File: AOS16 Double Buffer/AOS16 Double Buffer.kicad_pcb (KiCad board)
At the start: 4 copper layers, 47 x 72 mm, 50 parts, among them IC1 IS61WV3216BLL-12TLI, IC2 SN74LVC16245ADGVR, IC3 SN74LVC16245ADGVR, IC4 SN74LVC16245ADGVR, IC5 SN74LVC16245ADGVR, J1 Conn_01x02_Pin, J2 Conn_02x08_Top_Bottom, J3 Conn_02x08_Top_Bottom, J4 Conn_02x08_Top_Bottom, J5 Conn_02x08_Top_Bottom, J6 Conn_01x07_Pin, U1 74AHC1G08, U2 74AHC1G08, U3 74AHC1G32, U4 74AHC1G32, U5 74AHC1G04, U6 74AHC1G04, U7 74LS157

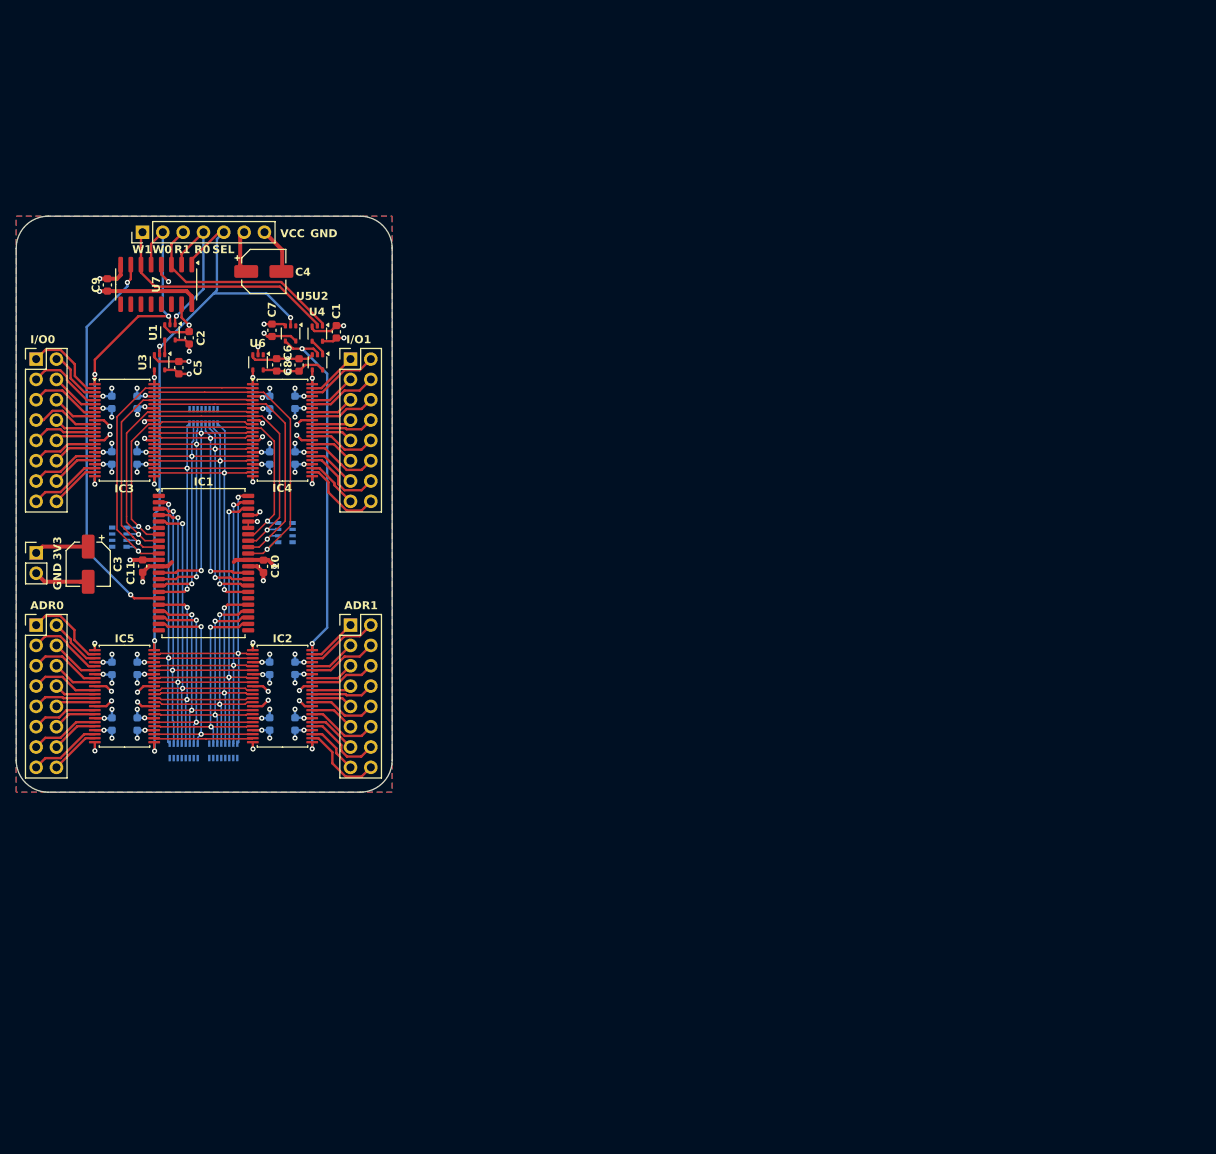
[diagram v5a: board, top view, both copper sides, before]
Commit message: Fixed double buffer logic families
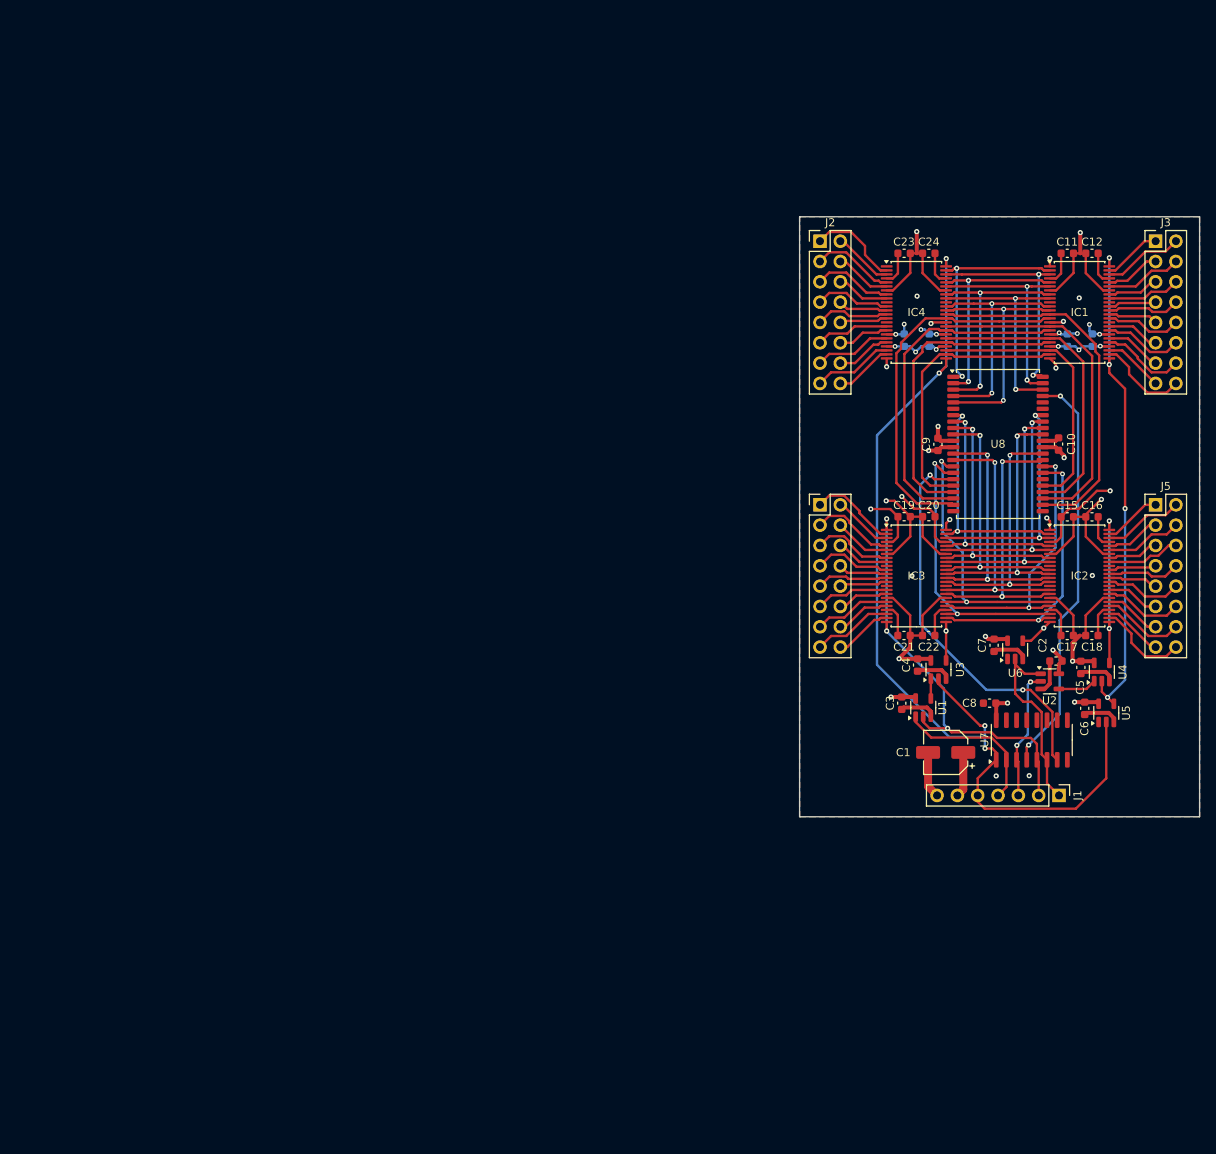
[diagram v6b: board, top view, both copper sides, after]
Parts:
- removed C27: 0.01uF, Capacitor_SMD:C_0603_1608Metric
- removed IC5: SN74LVC16245ADGVR, Package_SO:TSSOP-48_6.1x12.5mm_P0.5mm
- removed J6: Conn_01x07_Pin, Connector_PinHeader_2.54mm:PinHeader_1x07_P2.54mm_Vertical
- removed RN1, RN2, RN5: R_Pack08, Resistor_SMD:R_Array_Convex_8x0602
- removed RN3, RN4: R_Pack04, Resistor_SMD:R_Array_Convex_4x0603
- added U8: 71016S12PHG8, Package_SO:TSOP-II-44_10.16x18.41mm_P0.8mm, F.Cu at (146.7, 78.5)
- C1: value 0.1uF -> 100 uF; footprint Capacitor_SMD:C_0603_1608Metric -> Capacitor_SMD:CP_Elec_5x5.3
- C11: value 0.1uF -> 0.01uF
- C12, C15, C16, C17, C18, C19, C20, C21, C22, C23, C24: moved to F.Cu
- C3, C4: value 100 uF -> 0.1uF; footprint Capacitor_SMD:CP_Elec_5x5.3 -> Capacitor_SMD:C_0603_1608Metric
- IC1: value IS61WV3216BLL-12TLI -> SN74AHCT16245ADGGR; footprint Package_SO:TSOP-II-44_10.16x18.41mm_P0.8mm -> Package_SO:TSSOP-48_6.1x12.5mm_P0.5mm
- IC2, IC3, IC4: value SN74LVC16245ADGVR -> SN74AHCT16245ADGGR
- J1: value Conn_01x02_Pin -> Conn_01x07_Pin; footprint Connector_PinHeader_2.54mm:PinHeader_1x02_P2.54mm_Vertical -> Connector_PinHeader_2.54mm:PinHeader_1x07_P2.54mm_Vertical
- U1, U2: value 74AHC1G08 -> 74AHCT1G08; footprint Package_TO_SOT_SMD:SOT-353_SC-70-5 -> Package_TO_SOT_SMD:SOT-23-5
- U3, U4: value 74AHC1G32 -> 74AHCT1G32; footprint Package_TO_SOT_SMD:SOT-353_SC-70-5 -> Package_TO_SOT_SMD:SOT-23-5
- U5, U6: value 74AHC1G04 -> 74AHCT1G04; footprint Package_TO_SOT_SMD:SOT-353_SC-70-5 -> Package_TO_SOT_SMD:SOT-23-5
- U7: value 74LS157 -> 74LVC157
- moved J1 131.4 mm to (154.3, 122.4), turned to -90 degrees
- moved C18 124.5 mm to (158.5, 102.4), turned to 0 degrees
- moved U7 123.4 mm to (150.9, 115.5), turned to 90 degrees
- moved C16 123.4 mm to (158.5, 87.6), turned to 0 degrees
- moved C11 122.0 mm to (155.4, 54.6), turned to 180 degrees
- moved C17 119.9 mm to (155.4, 102.4), turned to 180 degrees
- moved C5 118.8 mm to (157.1, 106.4), turned to -90 degrees
- moved C2 115.6 mm to (154.0, 105.6), turned to 180 degrees
- moved C12 115.1 mm to (158.5, 54.6), turned to 0 degrees
- moved C24 114.5 mm to (138.1, 54.6), turned to 0 degrees
- moved IC1 113.9 mm to (156.9, 62.0)
- moved C14 113.5 mm to (158.5, 65.5)
- moved U5 112.4 mm to (160.3, 112.1), turned to 90 degrees
- moved J3 111.5 mm to (166.4, 53.1)
- moved C26 110.0 mm to (135.0, 65.5)
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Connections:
- C1 pad 1: VCC -> +5V
- C10 pad 1: +3.3V -> +5V
- C11 pad 1: +3.3V -> +5V
- C12 pad 1: +3.3V -> +5V
- C13 pad 1: +3.3V -> +5V
- C14 pad 1: +3.3V -> +5V
- C15 pad 1: +3.3V -> +5V
- C16 pad 1: +3.3V -> +5V
- C17 pad 1: +3.3V -> +5V
- C18 pad 1: +3.3V -> +5V
- C19 pad 1: +3.3V -> +5V
- C2 pad 1: VCC -> +5V
- C20 pad 1: +3.3V -> +5V
- C21 pad 1: +3.3V -> +5V
- C22 pad 1: +3.3V -> +5V
- C23 pad 1: +3.3V -> +5V
- C24 pad 1: +3.3V -> +5V
- C25 pad 1: +3.3V -> +5V
- C26 pad 1: +3.3V -> +5V
- C3 pad 1: +3.3V -> +5V
- C4 pad 1: VCC -> +5V
- C5 pad 1: VCC -> +5V
- C6 pad 1: VCC -> +5V
- C7 pad 1: VCC -> +5V
- C8 pad 1: VCC -> +5V
- C9 pad 1: VCC -> +5V
- IC1 pad 1: unconnected-(IC1-NC_1-Pad1) -> +5V
- IC1 pad 10: /ram/OUT0 -> GND
- IC1 pad 11: +3.3V -> /ram/INA6
- IC1 pad 12: GND -> /ram/INA7
- IC1 pad 13: /ram/OUT8 -> /ram/INA8
- IC1 pad 14: /ram/OUT10 -> /ram/INA9
- IC1 pad 15: /ram/OUT12 -> GND
- IC1 pad 16: /ram/OUT14 -> /ram/INA10
- IC1 pad 17: /W -> /ram/INA11
- IC1 pad 18: /pull_resistor/IN8 -> +5V
- IC1 pad 19: /pull_resistor/IN10 -> /ram/INA12
- IC1 pad 2: /pull_resistor/IN1 -> /ram/INA0
- IC1 pad 20: /pull_resistor/IN12 -> /ram/INA13
- IC1 pad 21: /pull_resistor/IN14 -> GND
- IC1 pad 22: unconnected-(IC1-NC_2-Pad22) -> /ram/INA14
- IC1 pad 23: unconnected-(IC1-NC_3-Pad23) -> /ram/INA15
- IC1 pad 24: /pull_resistor/IN13 -> +5V
- IC1 pad 25: /pull_resistor/IN11 -> /~{SEL}
- IC1 pad 26: /pull_resistor/IN9 -> /word_conn1/IN15
- IC1 pad 27: /pull_resistor/IN7 -> /word_conn1/IN14
- IC1 pad 28: unconnected-(IC1-NC_4-Pad28) -> GND
- IC1 pad 29: /ram/OUT15 -> /word_conn1/IN13
- IC1 pad 3: /pull_resistor/IN3 -> /ram/INA1
- IC1 pad 30: /ram/OUT13 -> /word_conn1/IN12
- IC1 pad 31: /ram/OUT11 -> +5V
- IC1 pad 32: /ram/OUT9 -> /word_conn1/IN11
- IC1 pad 33: +3.3V -> /word_conn1/IN10
- IC1 pad 35: /ram/OUT1 -> /word_conn1/IN9
- IC1 pad 36: /ram/OUT3 -> /word_conn1/IN8
- IC1 pad 37: /ram/OUT5 -> /word_conn1/IN7
- IC1 pad 38: /ram/OUT7 -> /word_conn1/IN6
- IC1 pad 4: /pull_resistor/IN5 -> GND
- IC1 pad 40: GND -> /word_conn1/IN5
- IC1 pad 41: /R -> /word_conn1/IN4
- IC1 pad 42: /pull_resistor/IN4 -> +5V
- IC1 pad 43: /pull_resistor/IN2 -> /word_conn1/IN3
- IC1 pad 44: /pull_resistor/IN0 -> /word_conn1/IN2
- IC1 pad 5: /pull_resistor/IN6 -> /ram/INA2
- IC1 pad 6: GND -> /ram/INA3
- IC1 pad 7: /ram/OUT6 -> +5V
- IC1 pad 8: /ram/OUT4 -> /ram/INA4
- IC1 pad 9: /ram/OUT2 -> /ram/INA5
- IC2 pad 1: +3.3V -> /W1
- IC2 pad 11: /pull_resistor/IN6 -> /ram/IO6
- IC2 pad 12: /pull_resistor/IN7 -> /ram/IO7
- IC2 pad 13: /pull_resistor/IN8 -> /ram/IO8
- IC2 pad 14: /pull_resistor/IN9 -> /ram/IO9
- IC2 pad 16: /pull_resistor/IN10 -> /ram/IO10
- IC2 pad 17: /pull_resistor/IN11 -> /ram/IO11
- IC2 pad 18: +3.3V -> +5V
- IC2 pad 19: /pull_resistor/IN12 -> /ram/IO12
- IC2 pad 2: /pull_resistor/IN0 -> /ram/IO0
- IC2 pad 20: /pull_resistor/IN13 -> /ram/IO13
- IC2 pad 22: /pull_resistor/IN14 -> /ram/IO14
- IC2 pad 23: /pull_resistor/IN15 -> /ram/IO15
- IC2 pad 24: +3.3V -> /W1
- IC2 pad 25: /~{SEL} -> /E1
- IC2 pad 26: /word_conn1/IN15 -> /word_conn3/IN15
- IC2 pad 27: /word_conn1/IN14 -> /word_conn3/IN14
- IC2 pad 29: /word_conn1/IN13 -> /word_conn3/IN13
- IC2 pad 3: /pull_resistor/IN1 -> /ram/IO1
- IC2 pad 30: /word_conn1/IN12 -> /word_conn3/IN12
- IC2 pad 31: +3.3V -> +5V
- IC2 pad 32: /word_conn1/IN11 -> /word_conn3/IN11
- IC2 pad 33: /word_conn1/IN10 -> /word_conn3/IN10
- IC2 pad 35: /word_conn1/IN9 -> /word_conn3/IN9
- IC2 pad 36: /word_conn1/IN8 -> /word_conn3/IN8
- IC2 pad 37: /word_conn1/IN7 -> /word_conn3/IN7
- IC2 pad 38: /word_conn1/IN6 -> /word_conn3/IN6
- IC2 pad 40: /word_conn1/IN5 -> /word_conn3/IN5
- IC2 pad 41: /word_conn1/IN4 -> /word_conn3/IN4
- IC2 pad 42: +3.3V -> +5V
- IC2 pad 43: /word_conn1/IN3 -> /word_conn3/IN3
- IC2 pad 44: /word_conn1/IN2 -> /word_conn3/IN2
- IC2 pad 46: /word_conn1/IN1 -> /word_conn3/IN1
- IC2 pad 47: /word_conn1/IN0 -> /word_conn3/IN0
- IC2 pad 48: /~{SEL} -> /E1
- IC2 pad 5: /pull_resistor/IN2 -> /ram/IO2
- IC2 pad 6: /pull_resistor/IN3 -> /ram/IO3
- IC2 pad 7: +3.3V -> +5V
- IC2 pad 8: /pull_resistor/IN4 -> /ram/IO4
- IC2 pad 9: /pull_resistor/IN5 -> /ram/IO5
- IC3 pad 1: /W0 -> /~{W0}
- IC3 pad 18: +3.3V -> +5V
- IC3 pad 24: /W0 -> /~{W0}
- IC3 pad 26: /ram/OUT15 -> /ram/IO15
- IC3 pad 27: /ram/OUT14 -> /ram/IO14
- IC3 pad 29: /ram/OUT13 -> /ram/IO13
- IC3 pad 30: /ram/OUT12 -> /ram/IO12
- IC3 pad 31: +3.3V -> +5V
- IC3 pad 32: /ram/OUT11 -> /ram/IO11
- IC3 pad 33: /ram/OUT10 -> /ram/IO10
- IC3 pad 35: /ram/OUT9 -> /ram/IO9
- IC3 pad 36: /ram/OUT8 -> /ram/IO8
- IC3 pad 37: /ram/OUT7 -> /ram/IO7
- IC3 pad 38: /ram/OUT6 -> /ram/IO6
- IC3 pad 40: /ram/OUT5 -> /ram/IO5
- IC3 pad 41: /ram/OUT4 -> /ram/IO4
- IC3 pad 42: +3.3V -> +5V
- IC3 pad 43: /ram/OUT3 -> /ram/IO3
- IC3 pad 44: /ram/OUT2 -> /ram/IO2
- IC3 pad 46: /ram/OUT1 -> /ram/IO1
- IC3 pad 47: /ram/OUT0 -> /ram/IO0
- IC3 pad 7: +3.3V -> +5V
- IC4 pad 1: /~{W1} -> GND
- IC4 pad 11: /ram/OUT6 -> /word_conn/IN6
- IC4 pad 12: /ram/OUT7 -> /word_conn/IN7
- IC4 pad 13: /ram/OUT8 -> /word_conn/IN8
- IC4 pad 14: /ram/OUT9 -> /word_conn/IN9
- IC4 pad 16: /ram/OUT10 -> /word_conn/IN10
- IC4 pad 17: /ram/OUT11 -> /word_conn/IN11
- IC4 pad 18: +3.3V -> +5V
- IC4 pad 19: /ram/OUT12 -> /word_conn/IN12
- IC4 pad 2: /ram/OUT0 -> /word_conn/IN0
- IC4 pad 20: /ram/OUT13 -> /word_conn/IN13
- IC4 pad 22: /ram/OUT14 -> /word_conn/IN14
- IC4 pad 23: /ram/OUT15 -> /word_conn/IN15
- IC4 pad 24: /~{W1} -> GND
- IC4 pad 25: /E1 -> /SEL
- IC4 pad 26: /word_conn3/IN15 -> /ram/INA15
- IC4 pad 27: /word_conn3/IN14 -> /ram/INA14
- IC4 pad 29: /word_conn3/IN13 -> /ram/INA13
- IC4 pad 3: /ram/OUT1 -> /word_conn/IN1
- IC4 pad 30: /word_conn3/IN12 -> /ram/INA12
- IC4 pad 31: +3.3V -> +5V
- IC4 pad 32: /word_conn3/IN11 -> /ram/INA11
- IC4 pad 33: /word_conn3/IN10 -> /ram/INA10
- IC4 pad 35: /word_conn3/IN9 -> /ram/INA9
- IC4 pad 36: /word_conn3/IN8 -> /ram/INA8
- IC4 pad 37: /word_conn3/IN7 -> /ram/INA7
- IC4 pad 38: /word_conn3/IN6 -> /ram/INA6
- IC4 pad 40: /word_conn3/IN5 -> /ram/INA5
- IC4 pad 41: /word_conn3/IN4 -> /ram/INA4
- IC4 pad 42: +3.3V -> +5V
- IC4 pad 43: /word_conn3/IN3 -> /ram/INA3
- IC4 pad 44: /word_conn3/IN2 -> /ram/INA2
- IC4 pad 46: /word_conn3/IN1 -> /ram/INA1
- IC4 pad 47: /word_conn3/IN0 -> /ram/INA0
- IC4 pad 48: /E1 -> /SEL
- IC4 pad 5: /ram/OUT2 -> /word_conn/IN2
- IC4 pad 6: /ram/OUT3 -> /word_conn/IN3
- IC4 pad 7: +3.3V -> +5V
- IC4 pad 8: /ram/OUT4 -> /word_conn/IN4
- IC4 pad 9: /ram/OUT5 -> /word_conn/IN5
- J1 pad 1: +3.3V -> /~{W1}
- J1 pad 2: GND -> /~{W0}
- U1 pad 1: /R0 -> /~{R0}
- U1 pad 2: /W0 -> /~{W0}
- U1 pad 5: VCC -> +5V
- U2 pad 1: /R1 -> /~{W1}
- U2 pad 2: /W1 -> /~{R1}
- U2 pad 5: VCC -> +5V
- U3 pad 5: VCC -> +5V
- U4 pad 5: VCC -> +5V
- U5 pad 5: VCC -> +5V
- U6 pad 2: /W1 -> /~{W1}
- U6 pad 4: /~{W1} -> /W1
- U6 pad 5: VCC -> +5V
- U7 pad 10: unconnected-(U7-I1c-Pad10) -> GND
- U7 pad 11: unconnected-(U7-I0c-Pad11) -> GND
- U7 pad 13: unconnected-(U7-I1d-Pad13) -> GND
- U7 pad 14: unconnected-(U7-I0d-Pad14) -> GND
- U7 pad 16: VCC -> +5V
- U7 pad 2: /R0 -> /~{R0}
- U7 pad 3: /R1 -> /~{R1}
- U7 pad 4: /R -> /~{R}
- U7 pad 5: /W0 -> /~{W0}
- U7 pad 6: /W1 -> /~{W1}
- U7 pad 7: /W -> /~{W}
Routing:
- net +5V: track 0.00 -> 156.7 mm, vias 0 -> 23
- net +3.3V: track 66.7 -> 0.00 mm, vias 36 -> 0
- net /~{W0}: track 0.00 -> 54.4 mm, vias 0 -> 3
- net /~{R}: track 0.00 -> 51.3 mm, vias 0 -> 2
- net /~{W}: track 0.00 -> 49.5 mm, vias 0 -> 2
- net /W: track 49.5 -> 0.00 mm, vias 2 -> 0
- net /ram/INA9: track 0.00 -> 46.2 mm
- net /ram/INA8: track 0.00 -> 45.9 mm
- net /W0: track 45.8 -> 0.00 mm, vias 3 -> 0
- net /pull_resistor/IN0: track 44.6 -> 0.00 mm, vias 2 -> 0
- net /pull_resistor/IN2: track 44.2 -> 0.00 mm, vias 2 -> 0
- net /pull_resistor/IN4: track 44.0 -> 0.00 mm, vias 2 -> 0
- net /pull_resistor/IN1: track 43.7 -> 0.00 mm, vias 2 -> 0
- net /pull_resistor/IN3: track 43.4 -> 0.00 mm, vias 2 -> 0
- net /pull_resistor/IN5: track 43.3 -> 0.00 mm, vias 2 -> 0
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- added copper zone on In1.Cu, net +5V
- added copper zone on In2.Cu, net GND
- removed copper zone on In2.Cu, net +3.3V
- removed copper zone on In1.Cu, net GND
- removed copper zone on In2.Cu, net VCC
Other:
- board size 47 x 72 mm -> 50 x 75 mm
- board text removed: "3V3"
- board text removed: "ADR0"
- board text removed: "ADR1"
- board text removed: "GND"
- board text removed: "I/O0"
- board text removed: "I/O1"
- board text removed: "R0"
- board text removed: "R1"
- board text removed: "SEL"
- board text removed: "VCC"
- board text removed: "W0"
- board text removed: "W1"

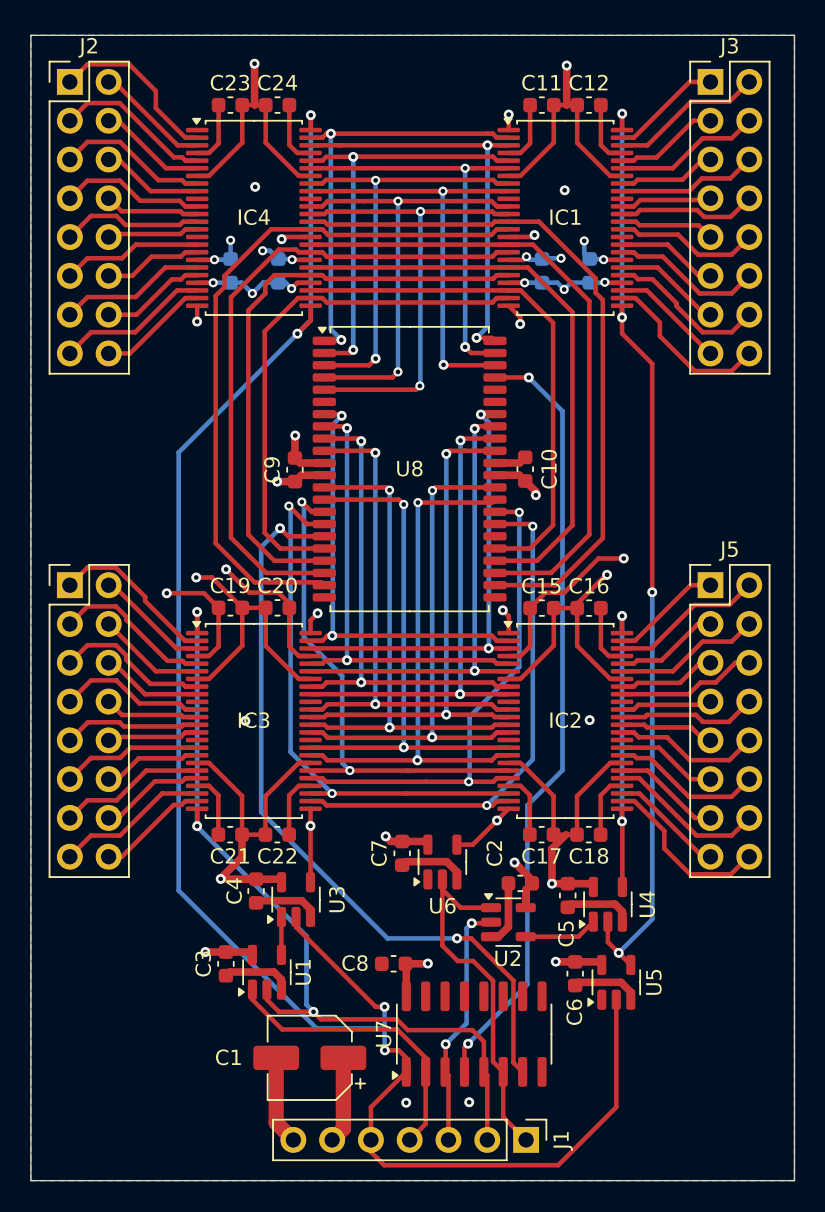
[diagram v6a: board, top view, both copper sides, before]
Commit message: Fixed tri-state buffer and completed double buffer PCB
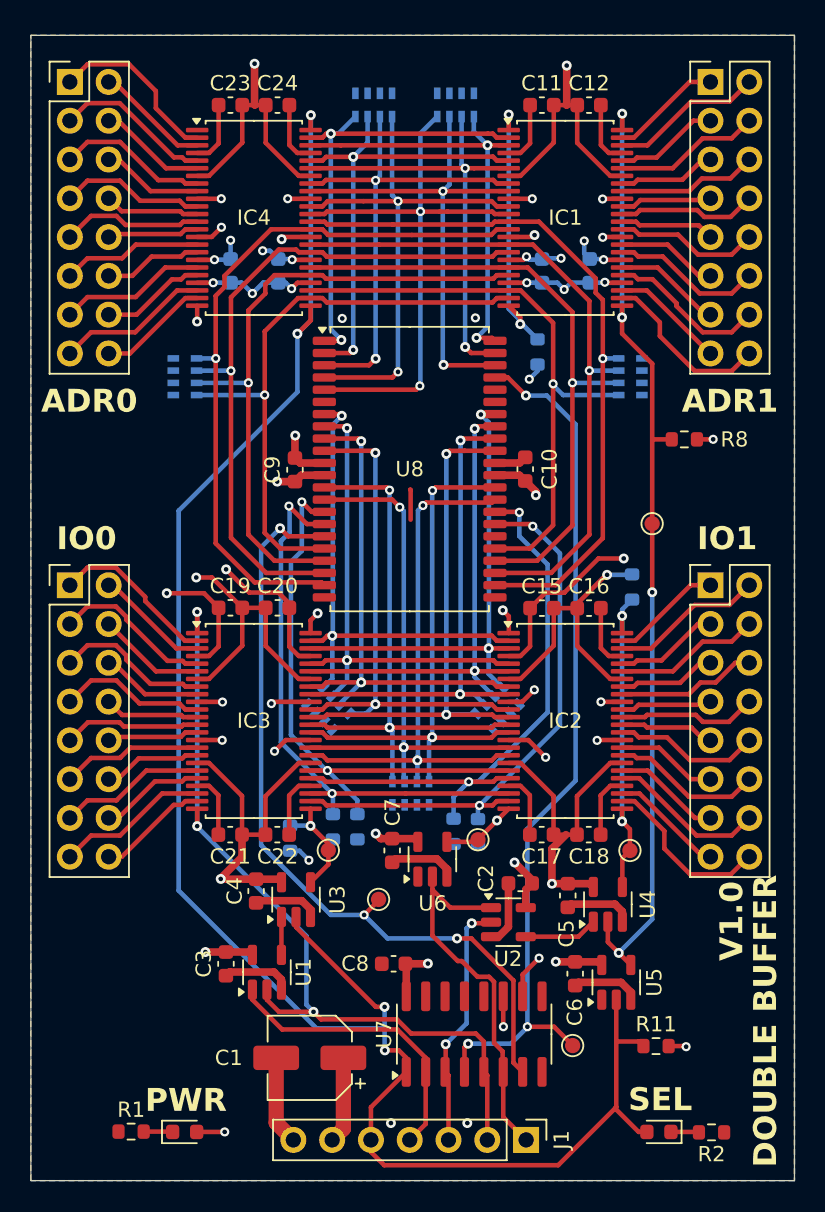
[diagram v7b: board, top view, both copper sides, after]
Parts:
- added D1: LED, LED_SMD:LED_0603_1608Metric, F.Cu at (132.0, 121.9)
- added D2: LED, LED_SMD:LED_0603_1608Metric, F.Cu at (163.0, 121.9)
- added R1: 100, Resistor_SMD:R_0603_1608Metric, F.Cu at (128.5, 121.9)
- added R10: 1k, Resistor_SMD:R_0603_1608Metric, B.Cu at (138.9, 102.6)
- added R11: 1k, Resistor_SMD:R_0603_1608Metric, F.Cu at (162.9, 116.3)
- added R2: 100, Resistor_SMD:R_0603_1608Metric, F.Cu at (166.5, 121.9)
- added R3: 1k, Resistor_SMD:R_0603_1608Metric, B.Cu at (141.7, 101.9)
- added R4: 1k, Resistor_SMD:R_0603_1608Metric, B.Cu at (143.3, 101.9)
- added R5: 1k, Resistor_SMD:R_0603_1608Metric, B.Cu at (149.6, 102.2)
- added R6: 1k, Resistor_SMD:R_0603_1608Metric, B.Cu at (151.2, 102.2)
- added R7: 1k, Resistor_SMD:R_0603_1608Metric, B.Cu at (155.1, 70.8)
- added R8: 1k, Resistor_SMD:R_0603_1608Metric, F.Cu at (164.7, 76.5)
- added R9: 1k, Resistor_SMD:R_0603_1608Metric, B.Cu at (161.3, 86.2)
- added RN1: R_Pack04, Resistor_SMD:R_Cat16-4, B.Cu at (144.4, 54.6)
- added RN2: R_Pack04, Resistor_SMD:R_Cat16-4, B.Cu at (149.7, 54.6)
- added RN3: R_Pack04, Resistor_SMD:R_Cat16-4, B.Cu at (132.0, 72.4)
- added RN4: R_Pack04, Resistor_SMD:R_Cat16-4, B.Cu at (161.2, 72.4)
- added RN5: R_Pack04, Resistor_SMD:R_Cat16-4, B.Cu at (141.4, 94.2)
- added RN6: R_Pack04, Resistor_SMD:R_Cat16-4, B.Cu at (146.8, 99.7)
- added RN7: R_Pack04, Resistor_SMD:R_Cat16-4, B.Cu at (152.5, 94.2)
- added TP1: ~{E0}, TestPoint:TestPoint_Pad_D1.0mm, F.Cu at (141.4, 103.4)
- added TP2: ~{E1}, TestPoint:TestPoint_Pad_D1.0mm, F.Cu at (161.2, 103.5)
- added TP3: ~{SEL}, TestPoint:TestPoint_Pad_D1.0mm, F.Cu at (162.6, 82.0)
- added TP4: W1, TestPoint:TestPoint_Pad_D1.0mm, F.Cu at (151.2, 102.7)
- added TP5: ~{R}, TestPoint:TestPoint_Pad_D1.0mm, F.Cu at (157.4, 116.2)
- added TP6: ~{W}, TestPoint:TestPoint_Pad_D1.0mm, F.Cu at (144.7, 106.7)
- IC1, IC2, IC3, IC4: value SN74AHCT16245ADGGR -> SN74AHCT16245DGVR
- moved C7 0.68 mm to (145.6, 103.5)
- moved U6 0.68 mm to (148.2, 104.0)
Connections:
- net /E0 renamed /~{E0}
- net /E1 renamed /~{E1}
- net /ram/INA0 renamed /RAM_INA0
- net /ram/INA1 renamed /RAM_INA1
- net /ram/INA10 renamed /RAM_INA10
- net /ram/INA11 renamed /RAM_INA11
- net /ram/INA12 renamed /RAM_INA12
- net /ram/INA13 renamed /RAM_INA13
- net /ram/INA14 renamed /RAM_INA14
- net /ram/INA15 renamed /RAM_INA15
- net /ram/INA2 renamed /RAM_INA2
- net /ram/INA3 renamed /RAM_INA3
- net /ram/INA4 renamed /RAM_INA4
- net /ram/INA5 renamed /RAM_INA5
- net /ram/INA6 renamed /RAM_INA6
- net /ram/INA7 renamed /RAM_INA7
- net /ram/INA8 renamed /RAM_INA8
- net /ram/INA9 renamed /RAM_INA9
- net /ram/IO0 renamed /RAM_IO0
- net /ram/IO1 renamed /RAM_IO1
- net /ram/IO10 renamed /RAM_IO10
- net /ram/IO11 renamed /RAM_IO11
- net /ram/IO12 renamed /RAM_IO12
- net /ram/IO13 renamed /RAM_IO13
- net /ram/IO14 renamed /RAM_IO14
- net /ram/IO15 renamed /RAM_IO15
- net /ram/IO2 renamed /RAM_IO2
- net /ram/IO3 renamed /RAM_IO3
- net /ram/IO4 renamed /RAM_IO4
- net /ram/IO5 renamed /RAM_IO5
- net /ram/IO6 renamed /RAM_IO6
- net /ram/IO7 renamed /RAM_IO7
- net /ram/IO8 renamed /RAM_IO8
- net /ram/IO9 renamed /RAM_IO9
- IC1 pad 1: +5V -> /tri-state buffer1/A2B
- IC1 pad 24: +5V -> /tri-state buffer1/A2B
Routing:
- net GND: track 125.9 -> 158.5 mm, vias 19 -> 33
- net /tri-state buffer1/A2B: track 0.00 -> 18.1 mm, vias 0 -> 2
- net /RAM_INA7: track 30.9 -> 37.6 mm
- net +5V: track 156.7 -> 162.6 mm, vias 23 -> 26
- net /~{R}: track 51.3 -> 57.1 mm, vias 2 -> 3
- net /RAM_INA6: track 29.4 -> 35.1 mm
- net /RAM_INA5: track 27.7 -> 32.8 mm
- net /RAM_IO13: track 33.8 -> 38.5 mm
- net /SEL: track 120.0 -> 124.6 mm
- net /RAM_INA14: track 34.5 -> 39.0 mm, vias 0 -> 1
- net /RAM_INA15: track 34.6 -> 39.1 mm, vias 0 -> 1
- net /RAM_INA4: track 28.4 -> 32.7 mm
- net /RAM_IO12: track 33.6 -> 37.3 mm
- net /RAM_IO0: track 29.1 -> 32.8 mm
- net /RAM_IO8: track 33.0 -> 36.6 mm
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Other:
- board text added: "5V"
- board text added: "ADR0"
- board text added: "ADR1"
- board text added: "DOUBLE BUFFER"
- board text added: "GND"
- board text added: "IO0"
- board text added: "IO1"
- board text added: "PWR"
- board text added: "SEL"
- board text added: "V1.0"
- board text added: "~{R0}"
- board text added: "~{R1}"
- board text added: "~{W0}"
- board text added: "~{W1}"
